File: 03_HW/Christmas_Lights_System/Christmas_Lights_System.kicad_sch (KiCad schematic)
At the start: 13 parts, among them IC1 PIC18F24Q10-I_SP, J1 Conn_01x02_Male, Q1 TIP42C, Q2 TIP42C, Q3 TIP42C, U1 LM7805_TO220

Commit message: -updated schematic -initial version of PCB layout
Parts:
- added D2: LED, Connector_PinHeader_2.54mm:PinHeader_1x02_P2.54mm_Vertical, symbol Device:LED
- added J2: Conn_01x04_Female, Connector:FanPinHeader_1x04_P2.54mm_Vertical, symbol Connector:Conn_01x04_Female
- added R4: 0.5k, Resistor_THT:R_Axial_DIN0411_L9.9mm_D3.6mm_P7.62mm_Vertical, symbol Device:R
- C3: footprint (none) -> Capacitor_THT:C_Axial_L3.8mm_D2.6mm_P7.50mm_Horizontal
- D1: footprint LED_THT:LED_D5.0mm-4_RGB -> Connector_PinHeader_2.54mm:PinHeader_1x04_P2.54mm_Vertical
- R1, R2: value R -> 0.43k; footprint (none) -> Resistor_THT:R_Axial_DIN0411_L9.9mm_D3.6mm_P7.62mm_Vertical
- R3: value R -> 0.43k; footprint Resistor_THT:R_Axial_DIN0309_L9.0mm_D3.2mm_P2.54mm_Vertical -> Resistor_THT:R_Axial_DIN0411_L9.9mm_D3.6mm_P7.62mm_Vertical
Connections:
- net +12V: now also R4.1
- net +5V: now also J2.1 (VCC)
- net GND: now also D2.1 (K), J2.4 (VSS)
- net at IC1.17 (RC6): now also J2.2 (RX)
- net at IC1.18 (RC7): now also J2.3 (TX)
- new net: D2.2 (A), R4.2
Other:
- moved on the sheet: C2, C3, J1, U1

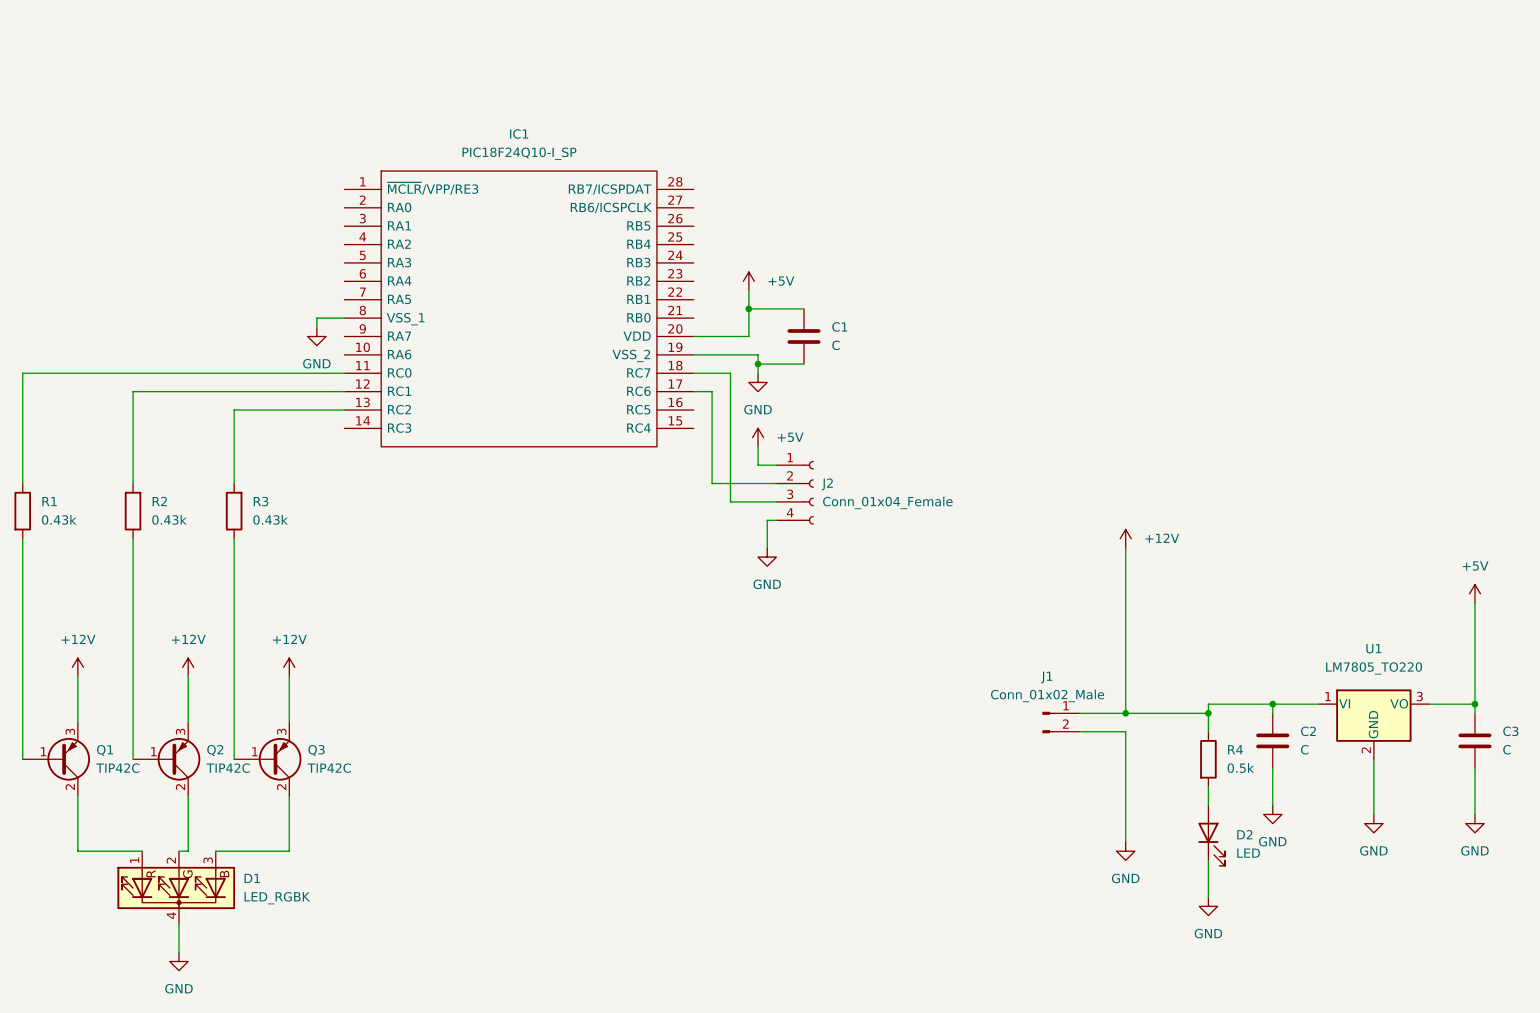
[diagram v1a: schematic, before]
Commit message: -added pwm and timer
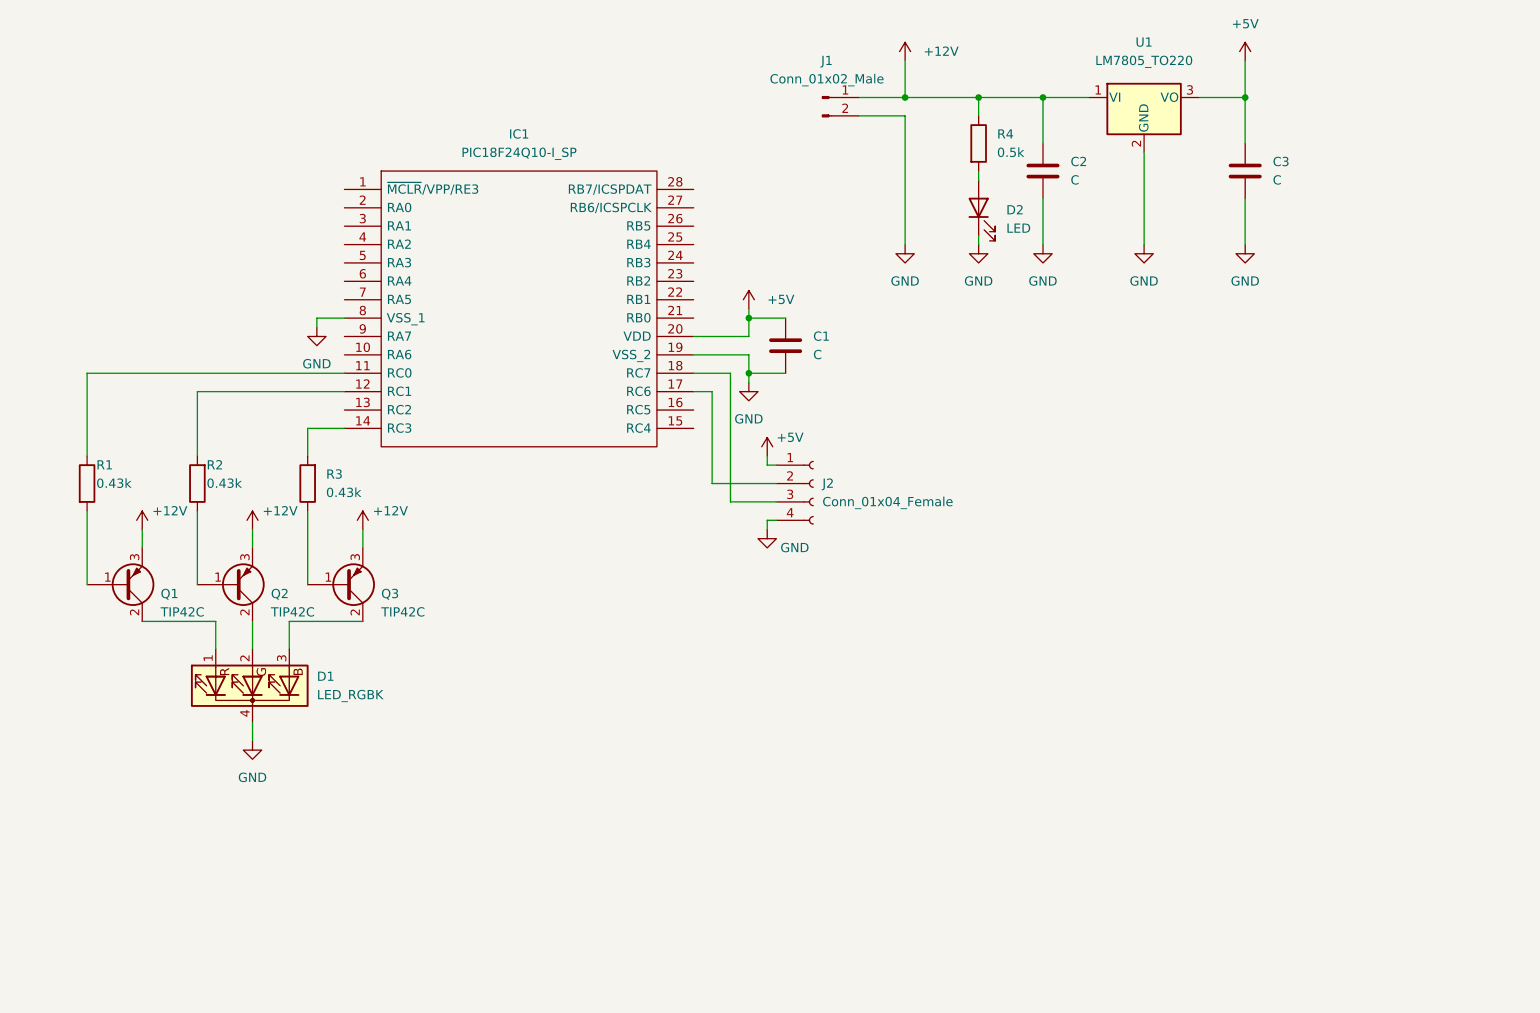
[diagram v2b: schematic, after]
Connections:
- net at IC1.13 (RC2): no longer R3.2
- net at IC1.14 (RC3): now also R3.2
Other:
- moved on the sheet: C1, C2, C3, D1, D2, J1, Q1, Q2, Q3, R1, R2, R3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
